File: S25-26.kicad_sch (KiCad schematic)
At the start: 15 parts, among them IC1 CMV4000-3E5M0PN

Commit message: Corrected LVDS
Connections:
- net LVDS Serialization/LVDS_10N: no longer names the net of IC1.B7 (OUT10_N)
- net LVDS Serialization/LVDS_10P: no longer names the net of IC1.B8 (OUT10_P)
- net LVDS Serialization/LVDS_11N: no longer names the net of IC1.C8 (OUT11_N)
- net LVDS Serialization/LVDS_11P: no longer names the net of IC1.C9 (OUT11_P)
- net LVDS Serialization/LVDS_12N: no longer names the net of IC1.A8 (OUT12_N)
- net LVDS Serialization/LVDS_12P: no longer names the net of IC1.A9 (OUT12_P)
- net LVDS Serialization/LVDS_13N: no longer names the net of IC1.B9 (OUT13_N)
- net LVDS Serialization/LVDS_13P: no longer names the net of IC1.B10 (OUT13_P)
- net LVDS Serialization/LVDS_14N: no longer names the net of IC1.D9 (OUT14_N)
- net LVDS Serialization/LVDS_14P: no longer names the net of IC1.D10 (OUT14_P)
- net LVDS Serialization/LVDS_15N: no longer names the net of IC1.A10 (OUT15_N)
- net LVDS Serialization/LVDS_15P: no longer names the net of IC1.A11 (OUT15_P)
- net LVDS Serialization/LVDS_16N: no longer names the net of IC1.C10 (OUT16_N)
- net LVDS Serialization/LVDS_16P: no longer names the net of IC1.C11 (OUT16_P)
- net LVDS Serialization/LVDS_9N: no longer names the net of IC1.D7 (OUT9_N)
- net LVDS Serialization/LVDS_9P: no longer names the net of IC1.D8 (OUT9_P)
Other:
- sheet LVDS Serialization ports: added none; removed DOUT10, DOUT11, DOUT12, DOUT13, DOUT14, DOUT15, DOUT16, DOUT9, LVDS_10N, LVDS_10P, LVDS_11N, LVDS_11P, LVDS_12N, LVDS_12P, LVDS_13N, LVDS_13P, LVDS_14N, LVDS_14P, LVDS_15N, LVDS_15P, LVDS_16N, LVDS_16P, LVDS_9N, LVDS_9P

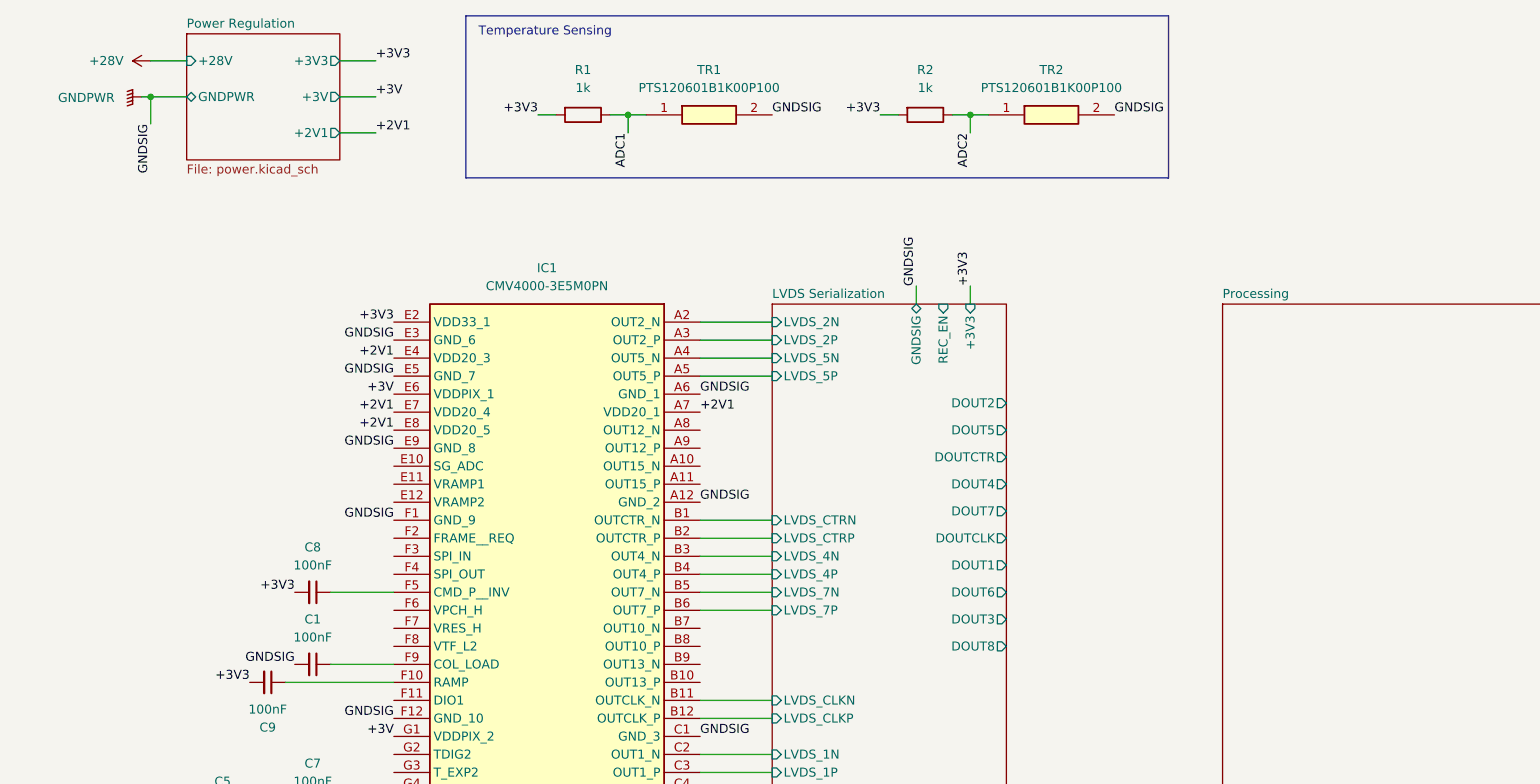
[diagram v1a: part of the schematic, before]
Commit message: Processing Updates
Added LVCMOS connections to MCU, added power regulation to MCU (NOT COMPLETE!)
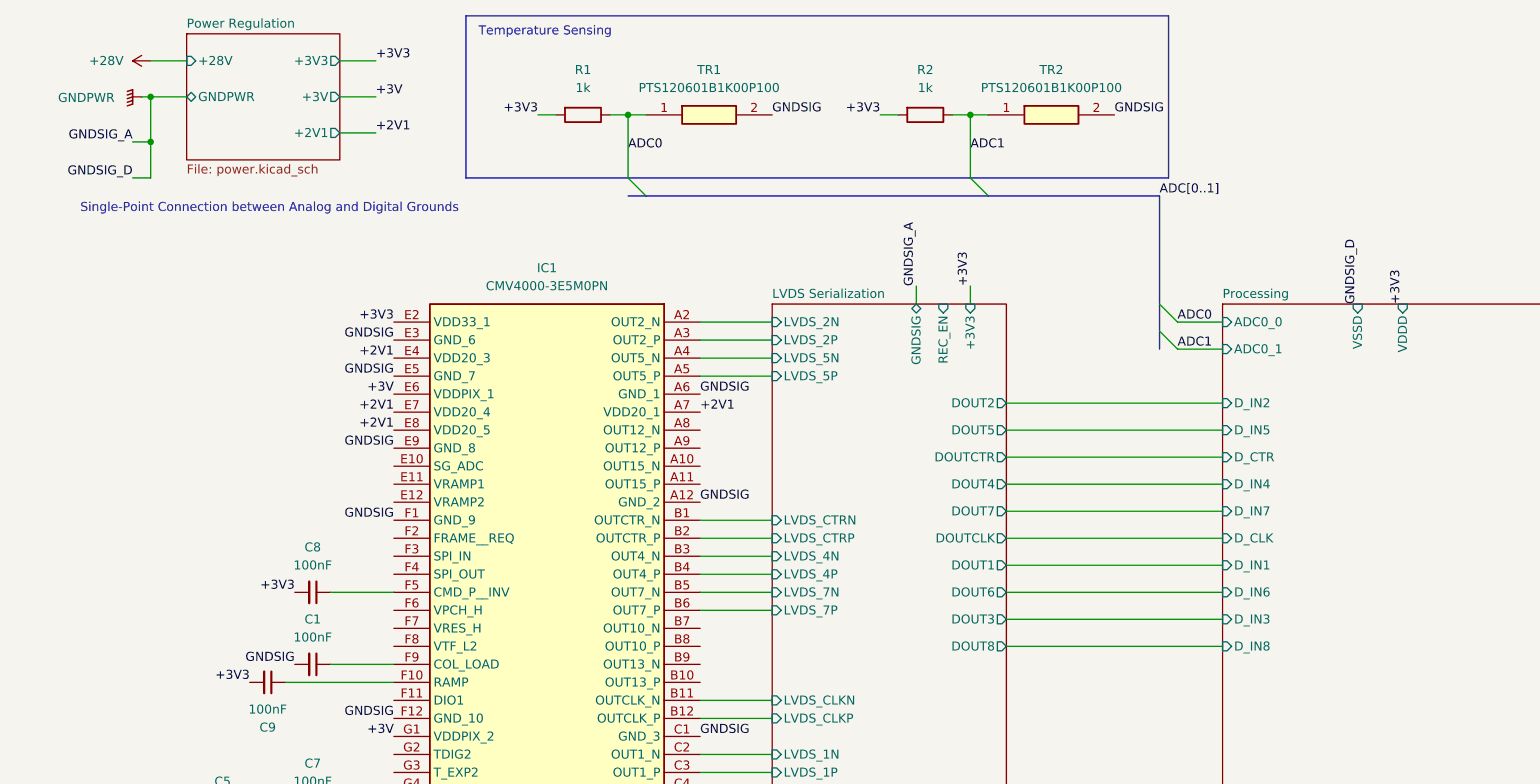
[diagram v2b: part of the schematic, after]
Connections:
- net ADC2 is gone; now on net ADC1: R2.1, TR2.1
- net ADC1: no longer R1.1, TR1.1
- net GNDPWR: no longer C1.2, C2.2, C3.2, C4.2, C5.2, C6.2, IC1.A12 (GND_2), IC1.A6 (GND_1), IC1.C1 (GND_3), IC1.C12 (GND_5), IC1.C6 (GND_4), IC1.E3 (GND_6), IC1.E5 (GND_7), IC1.E9 (GND_8), IC1.F1 (GND_9), IC1.F12 (GND_10), IC1.H7 (GND_11), TR1.2, TR2.2
- new net ADC0: R1.1, TR1.1
- new net GNDSIG: C1.2, C2.2, C3.2, C4.2, C5.2, C6.2, IC1.A12 (GND_2), IC1.A6 (GND_1), IC1.C1 (GND_3), IC1.C12 (GND_5), IC1.C6 (GND_4), IC1.E3 (GND_6), IC1.E5 (GND_7), IC1.E9 (GND_8), IC1.F1 (GND_9), IC1.F12 (GND_10), IC1.H7 (GND_11), TR1.2, TR2.2
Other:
- sheet Processing ports: added ADC0_0, ADC0_1, D_CLK, D_CTR, D_IN1, D_IN2, D_IN3, D_IN4, D_IN5, D_IN6, D_IN7, D_IN8, VDDD, VSSD; removed none
- note added: "Single-Point Connection between Analog and Digital Grounds"

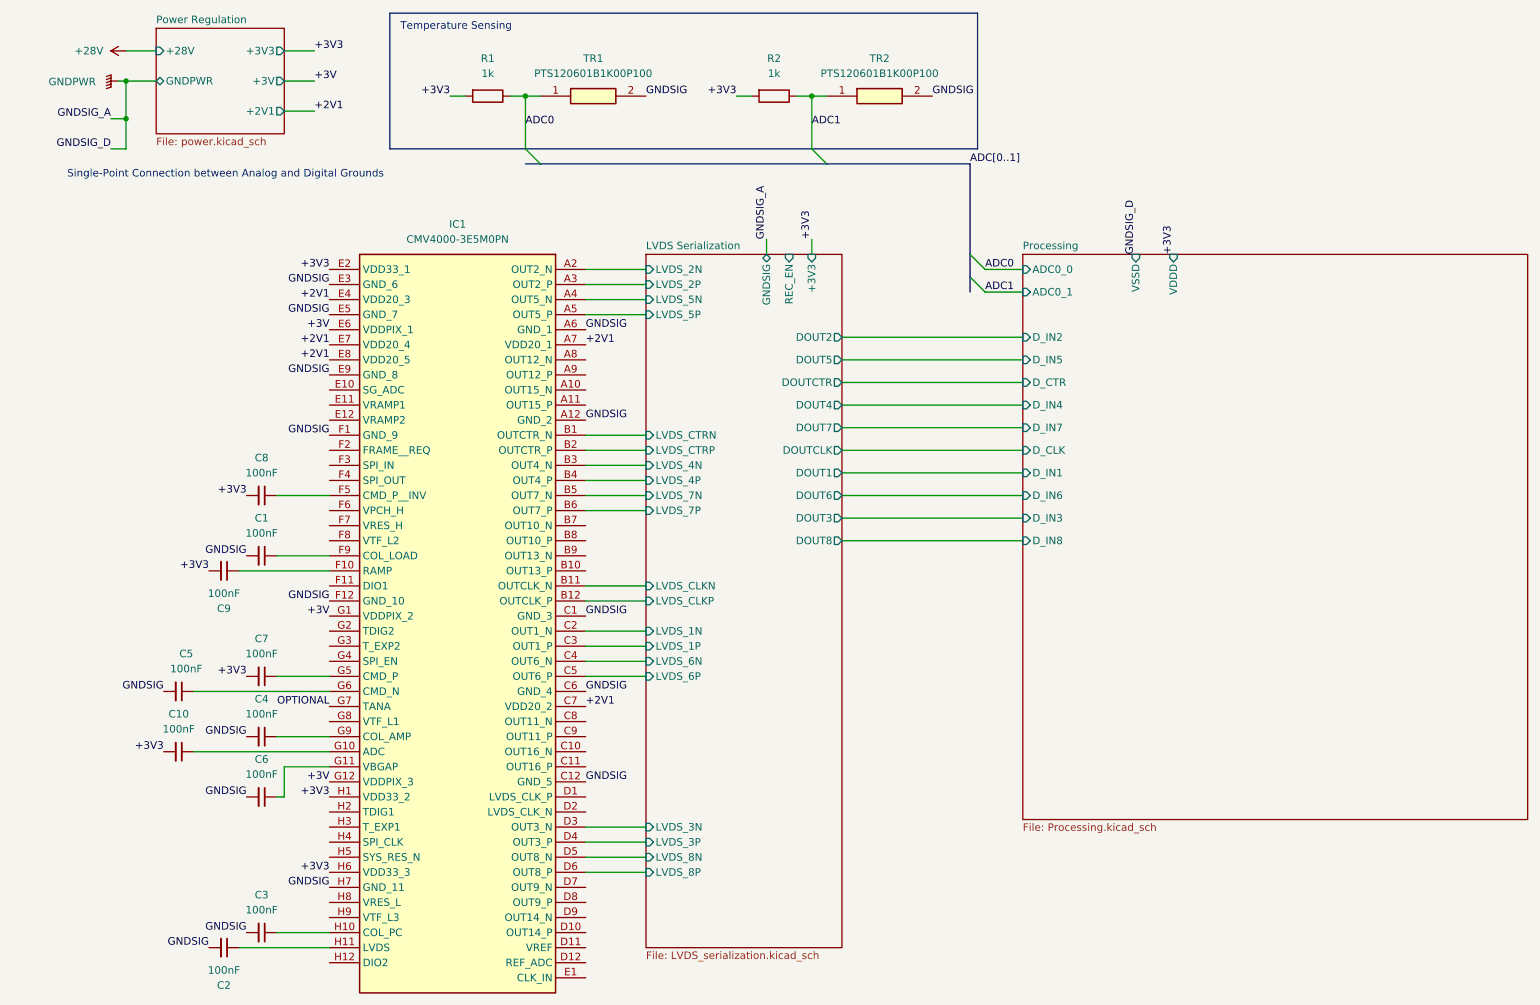
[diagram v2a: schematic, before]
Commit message: Added lots more connections
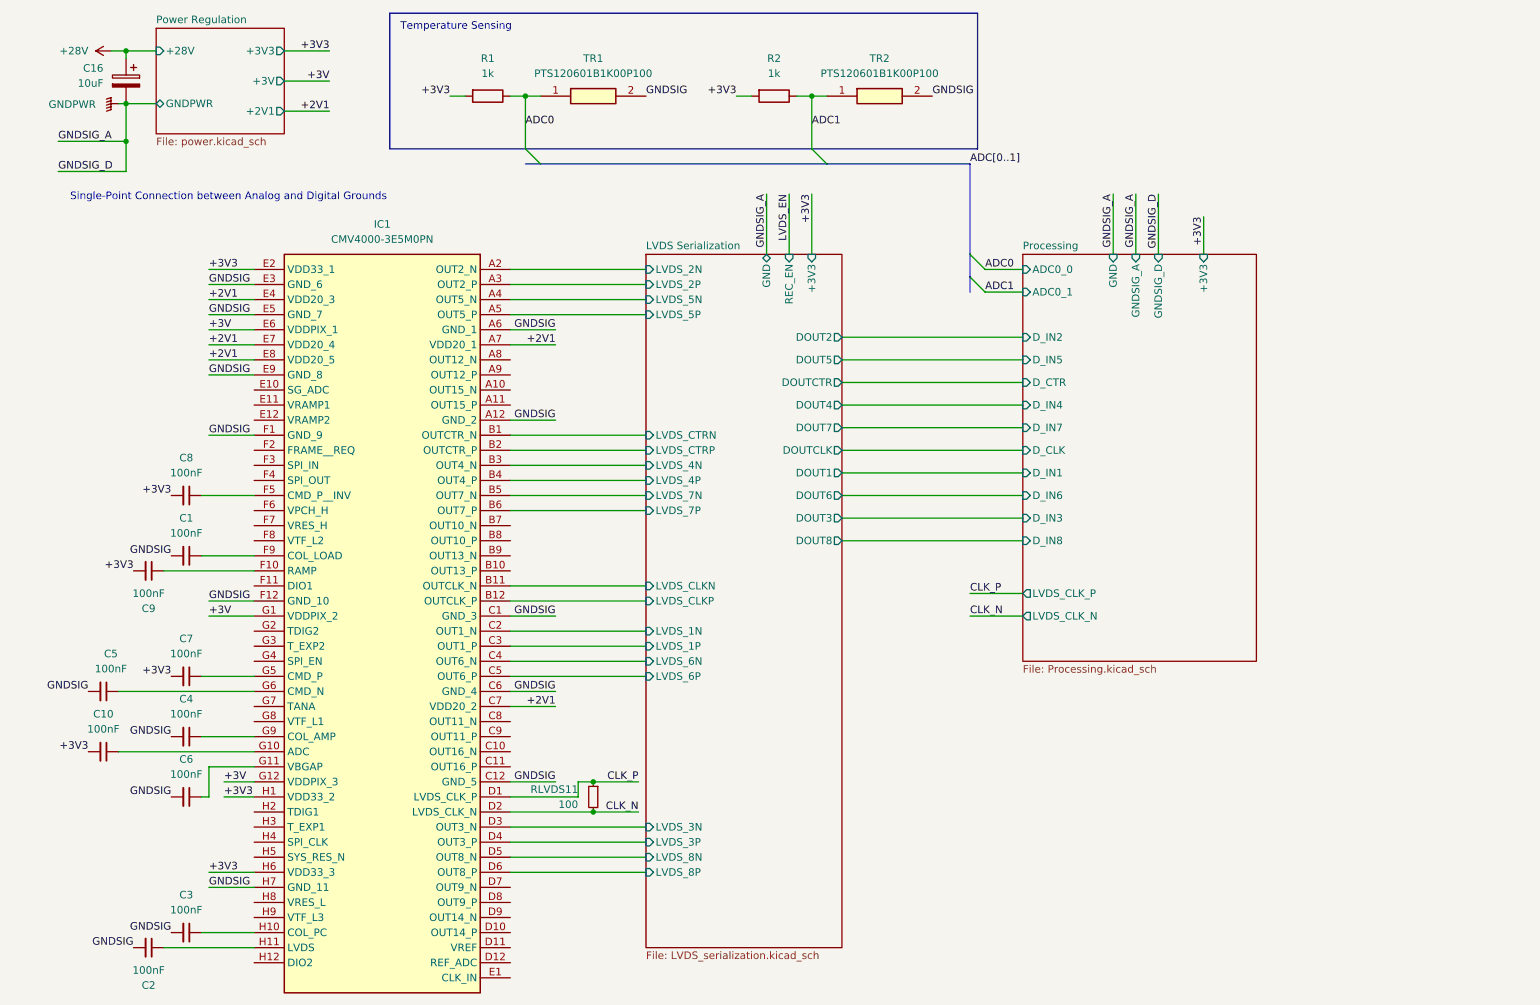
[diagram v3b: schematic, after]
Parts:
- added C16: 10uF, symbol Device:C_Polarized
- added RLVDS11: 100, symbol Device:R_Small
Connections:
- net +28V: now also C16.1
- net GNDPWR: now also C16.2
- net CLK_P: now reaches IC1.D1 (LVDS_CLK_P)
- net CLK_P: now also RLVDS11.1
- net CLK_N: now reaches IC1.D2 (LVDS_CLK_N)
- net CLK_N: now also RLVDS11.2
- net OPTIONAL: no longer names the net of IC1.G7 (TANA)
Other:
- sheet LVDS Serialization ports: added GND; removed GNDSIG
- sheet Processing ports: added +3V3, GND, GNDSIG_A, GNDSIG_D, LVDS_CLK_N, LVDS_CLK_P; removed VDDD, VSSD
- moved on the sheet: C1, C10, C2, C3, C4, C5, C6, C7, C8, C9, IC1
